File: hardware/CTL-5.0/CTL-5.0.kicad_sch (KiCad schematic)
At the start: 73 parts, among them J1 Conn_02x16_Top_Bottom, J3 Conn_01x03, J4 Conn_01x03, J5 Conn_02x06_Odd_Even, J6 Conn_01x04, J7 Conn_01x04, J8 Conn_01x04, K1 G5V-1, Q1 BCX56, Q2 BCX56, Q3 BCX56, Q4 BCX56, Q5 BCX56, Q6 BCX56, SW1 SW_Omron_B3FS, SW2 SW_Omron_B3FS, U1 AMS1117-3.3, U2 LM2576S-5, U3 LM2576S-12, U5 74LVC1G32, U6 PC817, U7 PC817, U8 USBLC6-2SC6

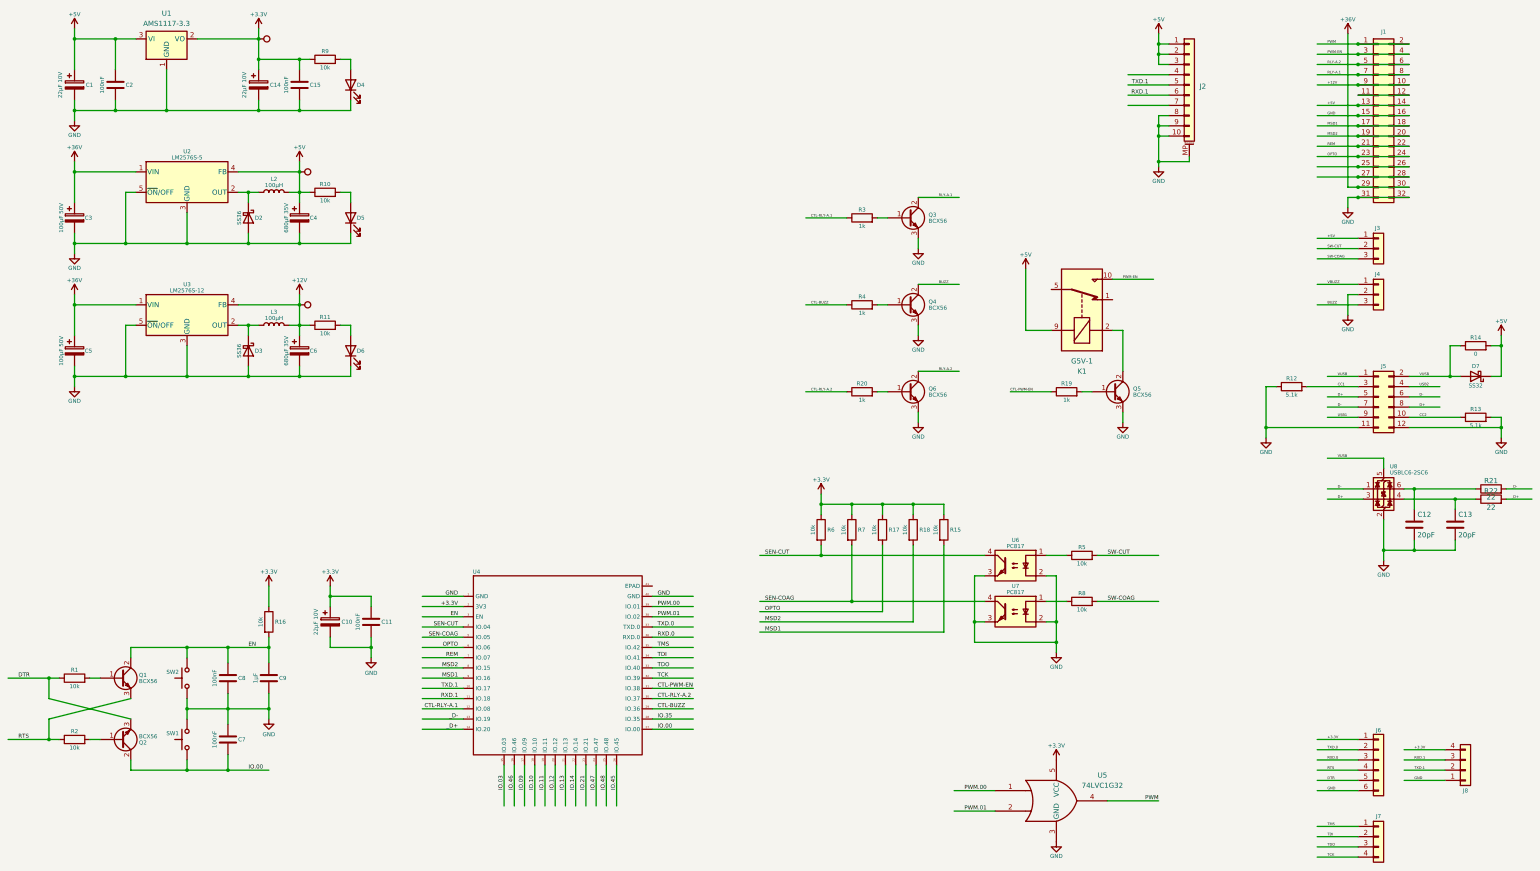
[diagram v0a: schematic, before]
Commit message: modified:   archive/Peripheral Migration ESP32S3-STM32H7.md 	new file:   archive/refferences/STM32H750xB pin definition.xlsx 	new file:   archive/refferences/STM32H750xB_pin_definition-TIM_LPTIM_HRTIM.xlsx 	new file:   archive/refferences/pin alternatives.xlsx 	new file:   firmware/core-h750/.cproject 	new file:   firmware/core-h750/.mxproject 	new file:   firmware/core-h750/.osx.project 	new file:   firmware/core-h750/.project 	new file:   firmware/core-h750/.settings/language.settings.xml 	new file:   firmware/core-h750/.settings/org.eclipse.core.resources.prefs 	new file:   firmware/core-h750/.settings/stm32cubeide.project.prefs 	new file:   firmware/core-h750/Debug/Drivers/STM32H7xx_HAL_Driver/Src/stm32h7xx_hal.cyclo 	new file:   firmware/core-h750/Debug/Drivers/STM32H7xx_HAL_Driver/Src/stm32h7xx_hal.su 	new file:   firmware/core-h750/Debug/Drivers/STM32H7xx_HAL_Driver/Src/stm32h7xx_hal_cortex.cyclo 	new file:   firmware/core-h750/Debug/Drivers/STM32H7xx_HAL_Driver/Src/stm32h7xx_hal_cortex.su 	new file:   firmware/core-h750/Debug/Drivers/STM32H7xx_HAL_Driver/Src/stm32h7xx_hal_dma.cyclo 	new file:   firmware/core-h750/Debug/Drivers/STM32H7xx_HAL_Driver/Src/stm32h7xx_hal_dma.su 	new file:   firmware/core-h750/Debug/Drivers/STM32H7xx_HAL_Driver/Src/stm32h7xx_hal_dma_ex.cyclo 	new file:   firmware/core-h750/Debug/Drivers/STM32H7xx_HAL_Driver/Src/stm32h7xx_hal_dma_ex.su 	new file:   firmware/core-h750/Debug/Drivers/STM32H7xx_HAL_Driver/Src/stm32h7xx_hal_exti.cyclo 	new file:   firmware/core-h750/Debug/Drivers/STM32H7xx_HAL_Driver/Src/stm32h7xx_hal_exti.su 	new file:   firmware/core-h750/Debug/Drivers/STM32H7xx_HAL_Driver/Src/stm32h7xx_hal_flash.cyclo 	new file:   firmware/core-h750/Debug/Drivers/STM32H7xx_HAL_Driver/Src/stm32h7xx_hal_flash.su 	new file:   firmware/core-h750/Debug/Drivers/STM32H7xx_HAL_Driver/Src/stm32h7xx_hal_flash_ex.cyclo 	new file:   firmware/core-h750/Debug/Drivers/STM32H7xx_HAL_Driver/Src/stm32h7xx_hal_flash_ex.su 	new file:   firmware/core-h750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
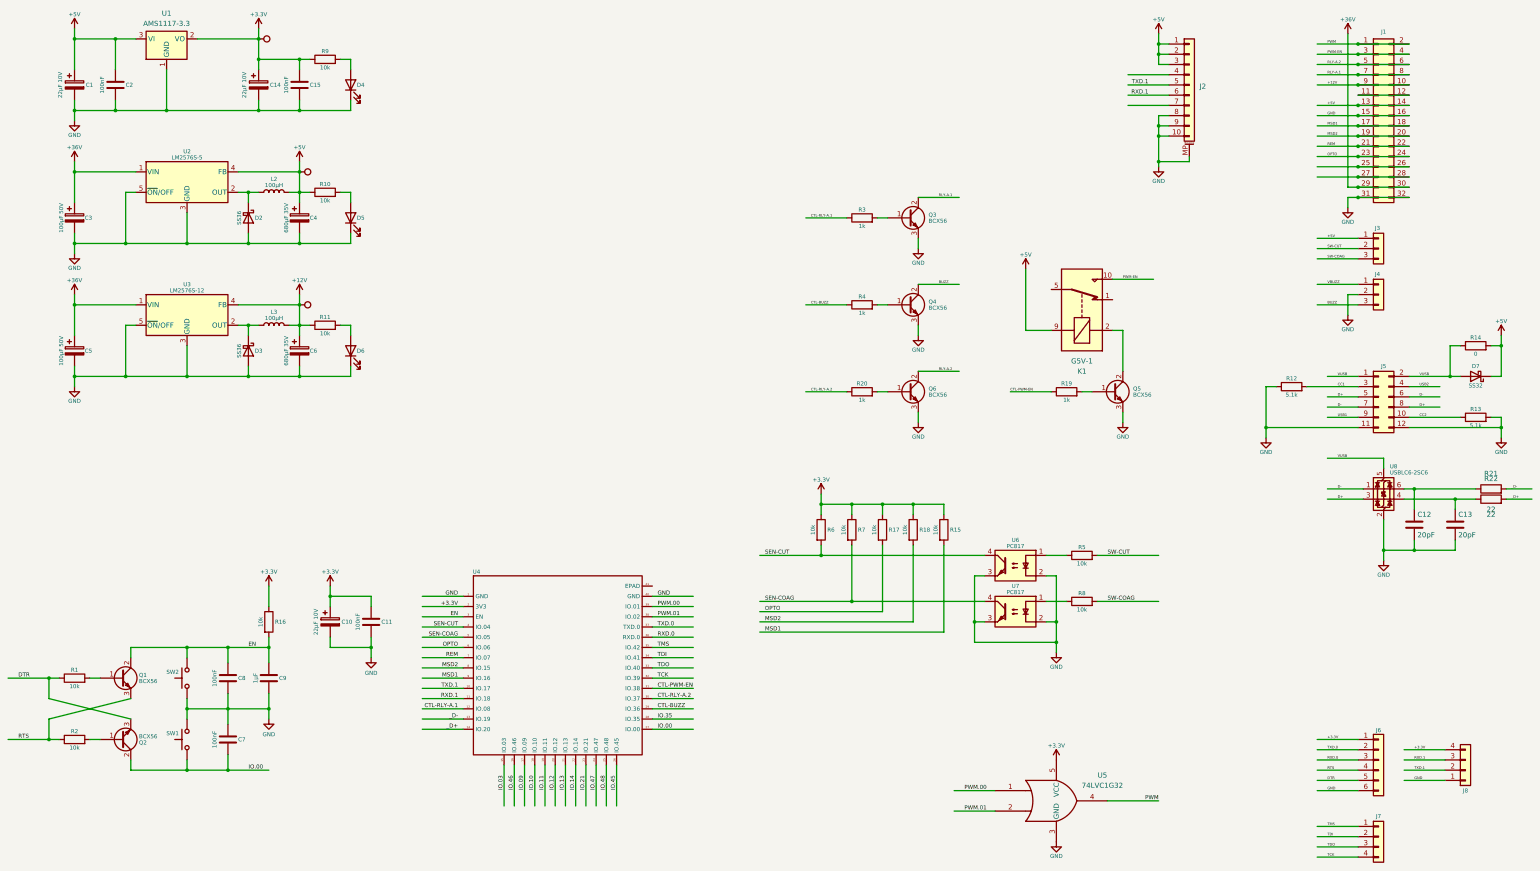
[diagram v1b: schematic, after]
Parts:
- J2, U4: value ~ -> (none)
